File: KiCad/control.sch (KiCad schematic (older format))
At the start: 33 parts

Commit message: saved from laptop and added new questions
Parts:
- U? (x6): symbol Comparator:LM393 -> Amp-Module-rescue:LM393-Comparator
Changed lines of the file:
@@
 DSP_IOUT1MON
 $Comp
-L Comparator:LM393 U?
+L Amp-Module-rescue:LM393-Comparator U?
 U 1 1 604E4013
 P 3800 5000
@@
 $EndComp
 $Comp
-L Comparator:LM393 U?
+L Amp-Module-rescue:LM393-Comparator U?
 U 2 1 604E4019
 P 3800 5500
@@
 $EndComp
 $Comp
-L Comparator:LM393 U?
+L Amp-Module-rescue:LM393-Comparator U?
 U 1 1 604E401F
 P 3800 6000
@@
 LM_TEMPMON34
 $Comp
-L Comparator:LM393 U?
+L Amp-Module-rescue:LM393-Comparator U?
 U 3 1 604E402A
 P 7600 5100
@@
 +5VDC
 $Comp
-L Comparator:LM393 U?
+L Amp-Module-rescue:LM393-Comparator U?
 U 3 1 604E4031
 P 7600 5450
@@
 Connection ~ 7250 5350
 $Comp
-L Comparator:LM393 U?
+L Amp-Module-rescue:LM393-Comparator U?
 U 2 1 604E4047
 P 3800 6500

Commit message: removed VU Meter sheet
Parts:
- added D? (x8): LED_Small, symbol Device:LED_Small
- added J? (x2): Conn_02x02_Odd_Even, symbol Connector_Generic:Conn_02x02_Odd_Even
- added R? (x10): R_Small, symbol Device:R_Small
- added U? (x15): LM393, symbol Amp-Module-rescue:LM393-Comparator
- added U?: CD4053B, symbol Analog_Switch:CD4053B
- added U? (x4): 74LS08, symbol 74xx:74LS08
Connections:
- net labels added: DSP_READY13, DSP_READY24, DSP_VOUT1MON, DSP_VOUT2MON, LM_READY1, LM_READY2, LM_READY3, LM_READY4, LM_VOUT1MON, LM_VOUT2MON, LM_VOUT3MON, LM_VOUT4MON, RESERVED_A, RESERVED_A1, RESERVED_A2, RESERVED_B, RESERVED_B1, RESERVED_B2, S1, S2
- wire segments 79 -> 193
- no-connect marks 3 -> 13
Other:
- note added: "READY"
- note added: "RESERVED"
- note added: "VOUT MONITOR"
- moved on the sheet: D?, Q?, R?, U?, U?A, U?B, U?C, U?E

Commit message: changed 4053 to DG419 & added negative latch
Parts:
- removed R? (x2): 100k, symbol Device:R_Small
- removed SW? (x2): SPDT, symbol Switch:SW_Push_SPDT
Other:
- moved on the sheet: D?, Q?, R?, U?A

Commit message: first commit
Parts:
- removed D? (x6): LED_Small, symbol Device:LED_Small
- removed Q? (x4): S9012, symbol Device:Q_PNP_BCE
- removed R? (x4): 10k, symbol Device:R_Small
- removed R? (x4): 150, symbol Device:R_Small
- removed R? (x2): R_Small, symbol Device:R_Small
- removed U?: 74LS08, symbol 74xx:74LS08
- added Q? (x3): Q_NPN_BCE, symbol Device:Q_NPN_BCE
- added R?: 100k, symbol Device:R_Small
- added R?: 33k, symbol Device:R_Small
- added R?: 10k, symbol Device:R_Small
- added U?: 74LS08, symbol 74xx:74LS08
- D? (x2): value LED_Small -> RED
- D? (x2): value LED_Small -> YELLOW
- D? (x2): value LED_Small -> GREEN
- R? (x2): value R_Small -> 23k
- R? (x2): value R_Small -> 33k
- R? (x2): value R_Small -> 36k
- R? (x2): value R_Small -> 75
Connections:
- net +5VDC: no longer D?.2 (A), D?.2 (A), D?.2 (A)
- net DSP_MUTE2: now also U?.2
- net DSP_VOUT1MON: now also U?.3 (+), U?.3 (+), U?.5 (+), R?.2, R?.2, R?.2; no longer U?.2 (-), U?.2 (-), U?.6 (-), U?.6 (-)
- net DSP_VOUT2MON: no longer U?.6 (-)
- net GND: now also Q?.3 (E), Q?.3 (E), Q?.3 (E)
- net LM_MUTE1: now also U?.3
- net mute2/OUT: now also U?.1
- net at U?.5 (+): no longer R?.1 (x2)
- net at R?.2, U?.3 (+): now also R?.1
- net at U?.1: now also D?.2 (A); no longer D?.1 (K)
- net at R?.1, R?.2: now also U?.2 (-); no longer U?.3 (+)
- net at R?.1, R?.2: now also U?.6 (-); no longer U?.5 (+)
- net at U?.7: now also D?.2 (A); no longer D?.1 (K)
- net at R?.2: now also R?.1, U?.2 (-); no longer U?.3 (+)
- net at D?.1 (K): now also Q?.2 (C); no longer U?.1
- new net: D?.1 (K), Q?.2 (C) (x2)
- new net: D?.2 (A), U?.1
- new net: Q?.1 (B), R?.1 (x3)
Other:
- moved on the sheet: D?, J?, R?, U?, U?A, U?B, U?C, U?D, U?E

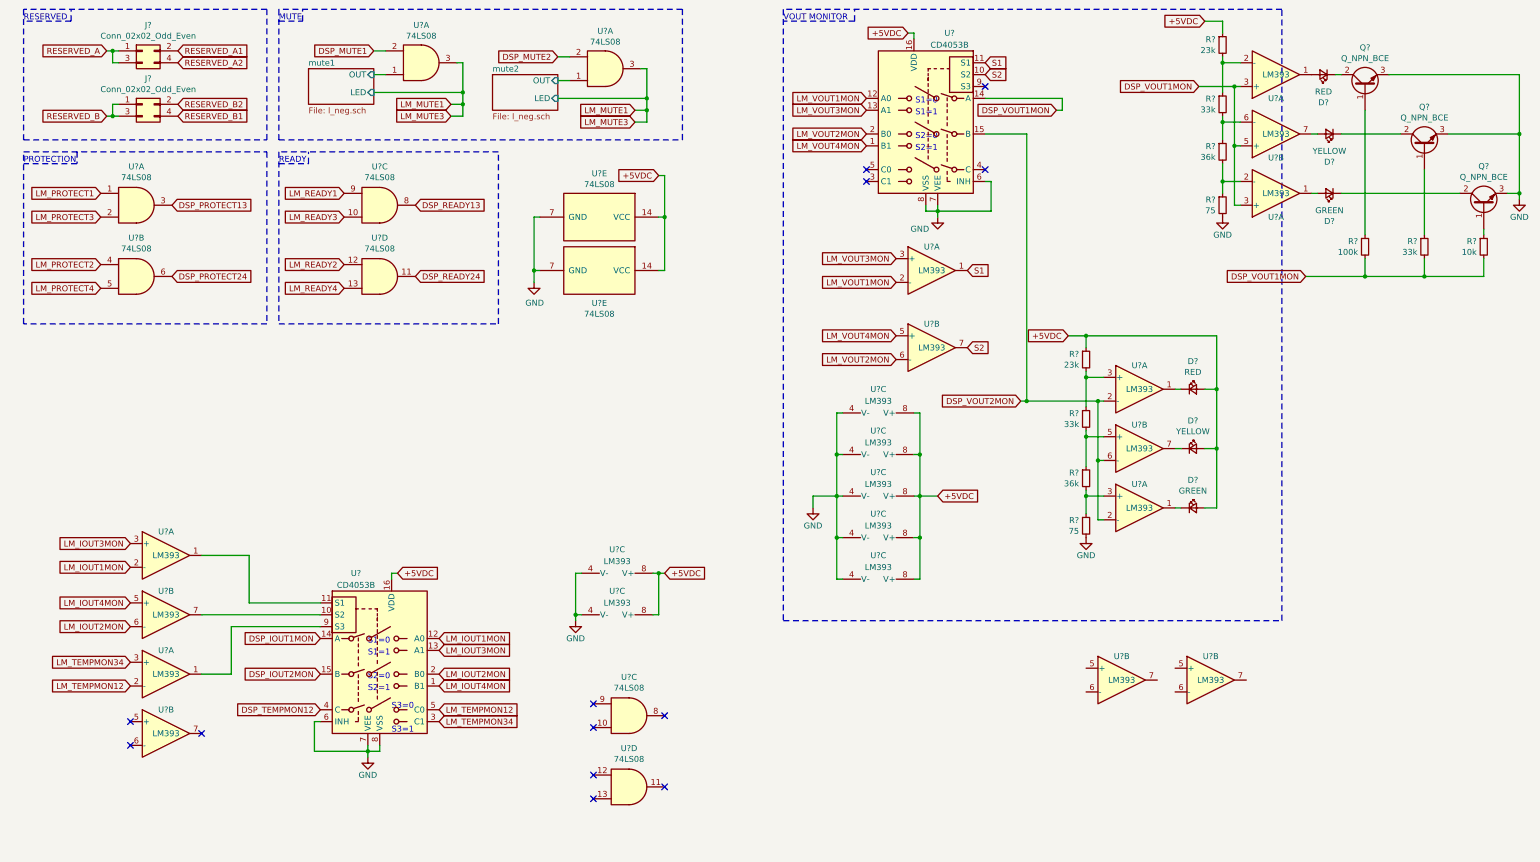
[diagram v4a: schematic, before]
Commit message: added custom VU meter
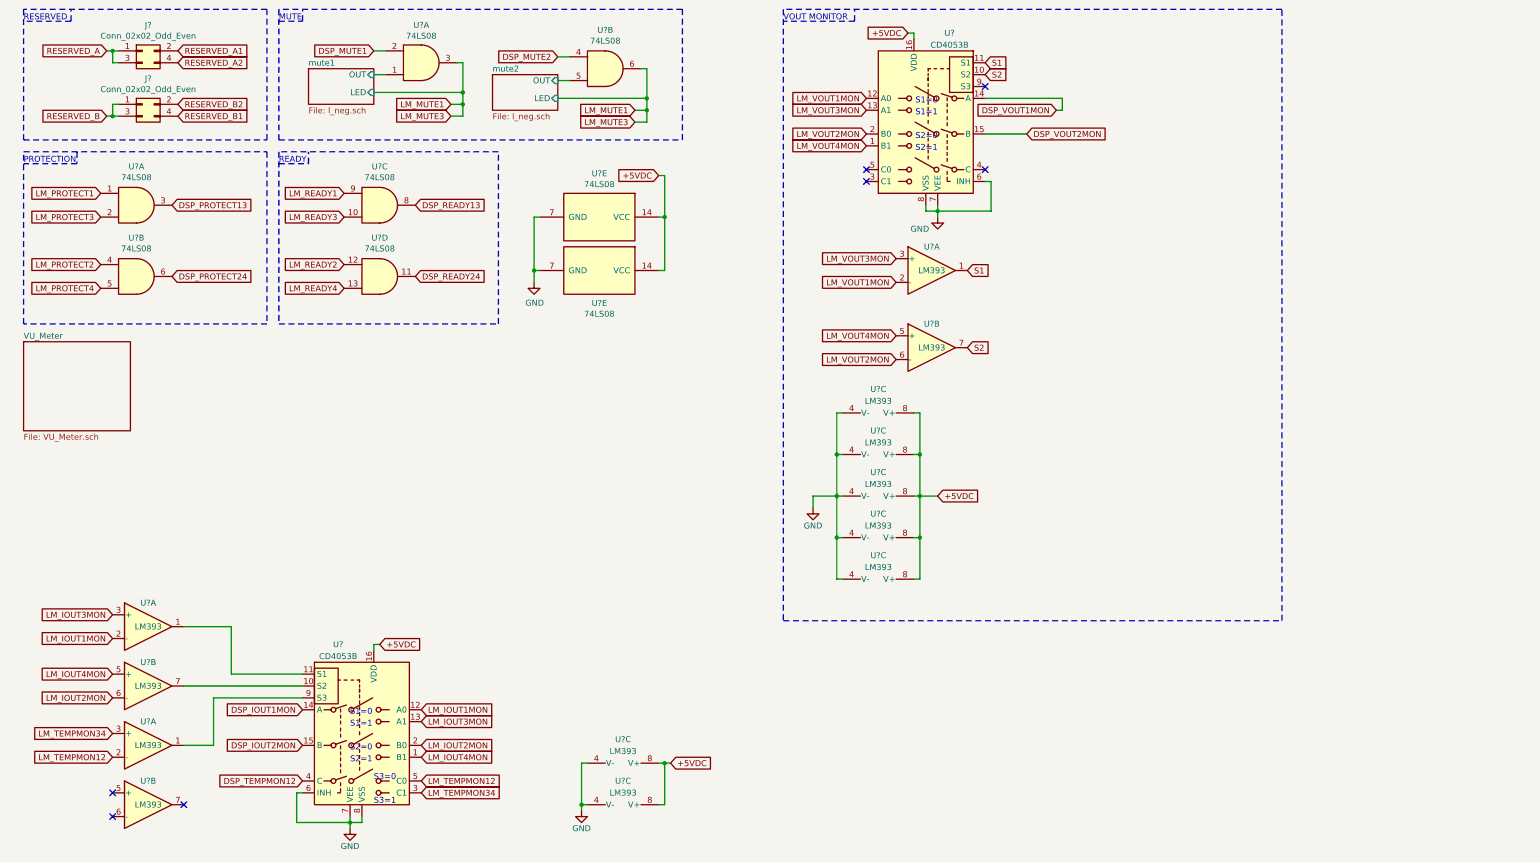
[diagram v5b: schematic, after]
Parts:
- removed D? (x2): RED, symbol Device:LED_Small
- removed D? (x2): YELLOW, symbol Device:LED_Small
- removed D? (x2): GREEN, symbol Device:LED_Small
- removed Q? (x3): Q_NPN_BCE, symbol Device:Q_NPN_BCE
- removed R? (x2): 23k, symbol Device:R_Small
- removed R? (x3): 33k, symbol Device:R_Small
- removed R? (x2): 36k, symbol Device:R_Small
- removed R? (x2): 75, symbol Device:R_Small
- removed R?: 100k, symbol Device:R_Small
- removed R?: 10k, symbol Device:R_Small
- removed U? (x8): LM393, symbol Amp-Module-rescue:LM393-Comparator
- removed U? (x3): 74LS08, symbol 74xx:74LS08
- added U?: 74LS08, symbol 74xx:74LS08
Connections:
- net DSP_MUTE2: now also U?.4
- net LM_MUTE1: now also U?.6
- net mute2/OUT: now also U?.5
- no-connect marks 13 -> 7
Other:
- moved on the sheet: U?, U?A, U?B, U?C

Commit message: first single IDC commit
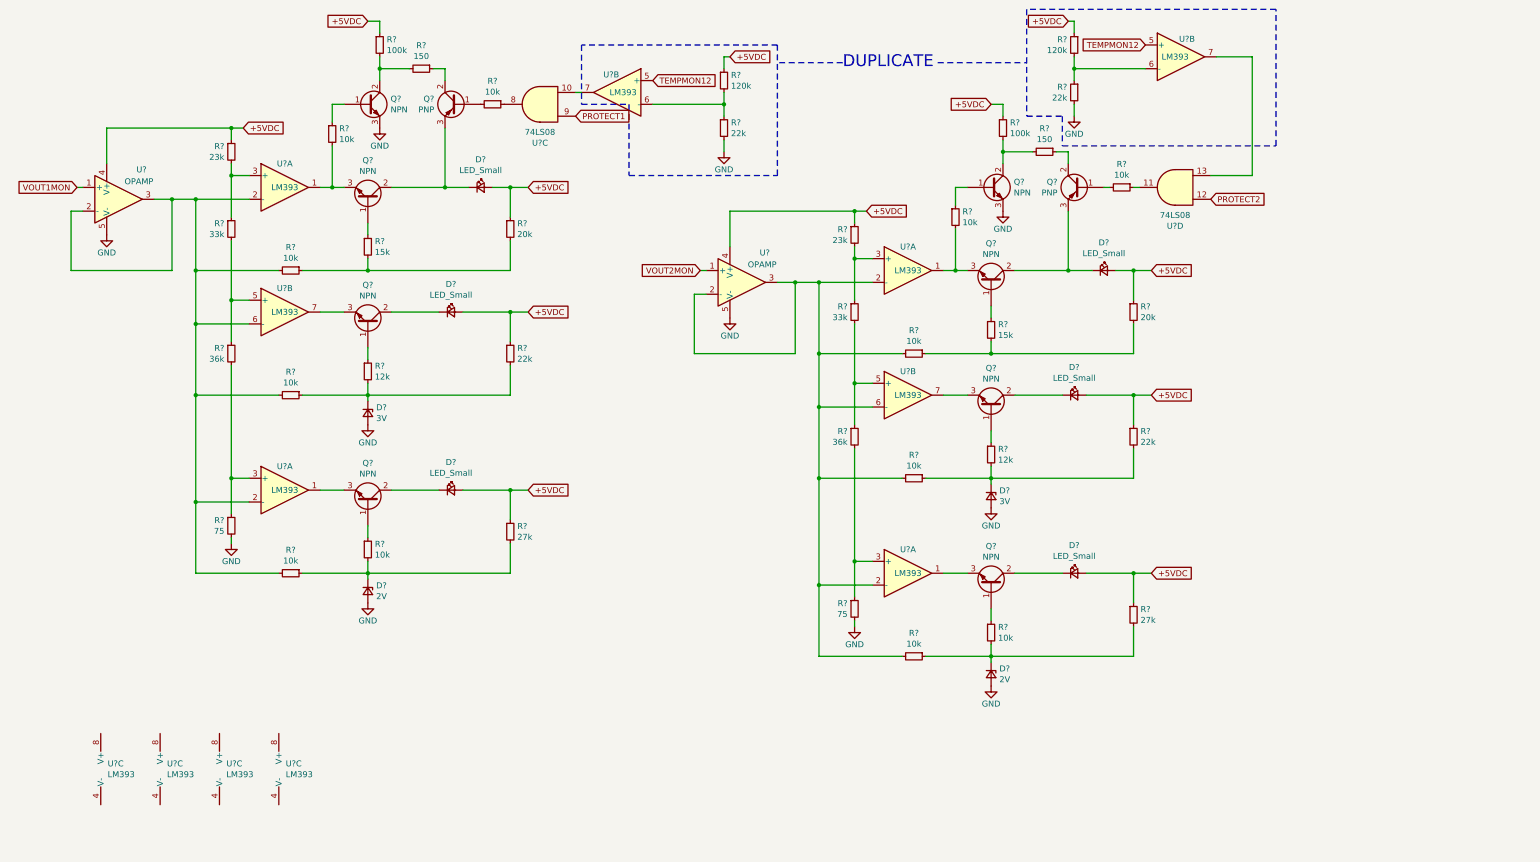
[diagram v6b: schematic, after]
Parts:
- removed J? (x2): Conn_02x02_Odd_Even, symbol Connector_Generic:Conn_02x02_Odd_Even
- removed U? (x8): 74LS08, symbol 74xx:74LS08
- removed U? (x2): CD4053B, symbol Analog_Switch:CD4053B
- removed U? (x13): LM393, symbol Amp-Module-rescue:LM393-Comparator
- added D? (x6): LED_Small, symbol Device:LED_Small
- added D? (x2): 3V, symbol Device:D_Zener_Small
- added D? (x2): 2V, symbol Device:D_Zener_Small
- added Q? (x8): NPN, symbol Device:Q_NPN_BCE
- added Q? (x2): PNP, symbol Device:Q_PNP_BCE
- added R? (x2): 75, symbol Device:R_Small
- added R? (x2): 20k, symbol Device:R_Small
- added R? (x2): 15k, symbol Device:R_Small
- added R? (x2): 23k, symbol Device:R_Small
- added R? (x12): 10k, symbol Device:R_Small
- added R? (x2): 100k, symbol Device:R_Small
- added R? (x2): 150, symbol Device:R_Small
- added R? (x4): 22k, symbol Device:R_Small
- added R? (x2): 12k, symbol Device:R_Small
- added R? (x2): 33k, symbol Device:R_Small
- added R? (x2): 27k, symbol Device:R_Small
- added R? (x2): 36k, symbol Device:R_Small
- added R? (x2): 120k, symbol Device:R_Small
- added U? (x12): LM393, symbol Amp-Module-rescue:LM393-Comparator
- added U? (x2): OPAMP, symbol pspice:OPAMP
- added U? (x2): 74LS08, symbol 74xx:74LS08
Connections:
- net +5VDC: now also D?.2 (A), D?.2 (A), D?.2 (A), D?.2 (A), D?.2 (A), D?.2 (A), R?.1, R?.1, R?.1, R?.1, R?.1, R?.1, R?.1, R?.1, R?.1, R?.1, R?.1, R?.1, U?.4 (V+), U?.4 (V+)
- net GND: now also D?.2 (A), D?.2 (A), D?.2 (A), D?.2 (A), Q?.3 (E), Q?.3 (E), R?.2, R?.2, R?.2, R?.2, U?.5 (V-), U?.5 (V-)
- new net: Q?.3 (E), R?.2, U?.1 (x2)
- new net: R?.2, R?.2, R?.2, U?.2 (-), U?.2 (-), U?.2 (-), U?.3, U?.6 (-) (x2)
- new net: R?.1, R?.2, U?.3 (+) (x4)
- new net: R?.1, R?.2, U?.5 (+) (x2)
- new net: Q?.3 (E), U?.7 (x2)
- new net: D?.1 (K), Q?.2 (C), Q?.3 (E) (x2)
- new net: Q?.3 (E), U?.1 (x2)
- new net: Q?.1 (B), R?.1 (x8)
- new net: R?.1, R?.2, R?.2 (x2)
- new net: Q?.2 (C), R?.2, R?.2 (x2)
- new net: Q?.2 (C), R?.1 (x2)
- new net: Q?.1 (B), R?.2 (x2)
- new net: R?.1, U?.8
- new net: D?.1 (K), Q?.2 (C) (x4)
- new net: D?.1 (K), R?.1, R?.2, R?.2 (x4)
- new net: R?.1, R?.2, U?.6 (-) (x2)
- new net: U?.10, U?.7
- new net: R?.1, U?.11
- new net: U?.13, U?.7
- new net PROTECT1: U?.9
- new net PROTECT2: U?.12
- new net TEMPMON12: U?.5 (+), U?.5 (+)
- new net VOUT1MON: U?.1 (+)
- new net VOUT2MON: U?.1 (+)
- no-connect marks 7 -> 0
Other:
- note added: "DUPLICATE"
- note removed: "MUTE"
- note removed: "PROTECTION"
- note removed: "READY"
- note removed: "RESERVED"
- note removed: "S1=0"
- note removed: "S1=1"
- note removed: "S2=0"
- note removed: "S2=1"
- note removed: "S3=0"
- note removed: "S3=1"
- note removed: "VOUT MONITOR"
